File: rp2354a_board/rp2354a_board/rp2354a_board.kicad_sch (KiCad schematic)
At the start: 10 parts, among them J1 USB_B_Micro, U1 RP2350_60QFN, U2 NCP1117-3.3_SOT223

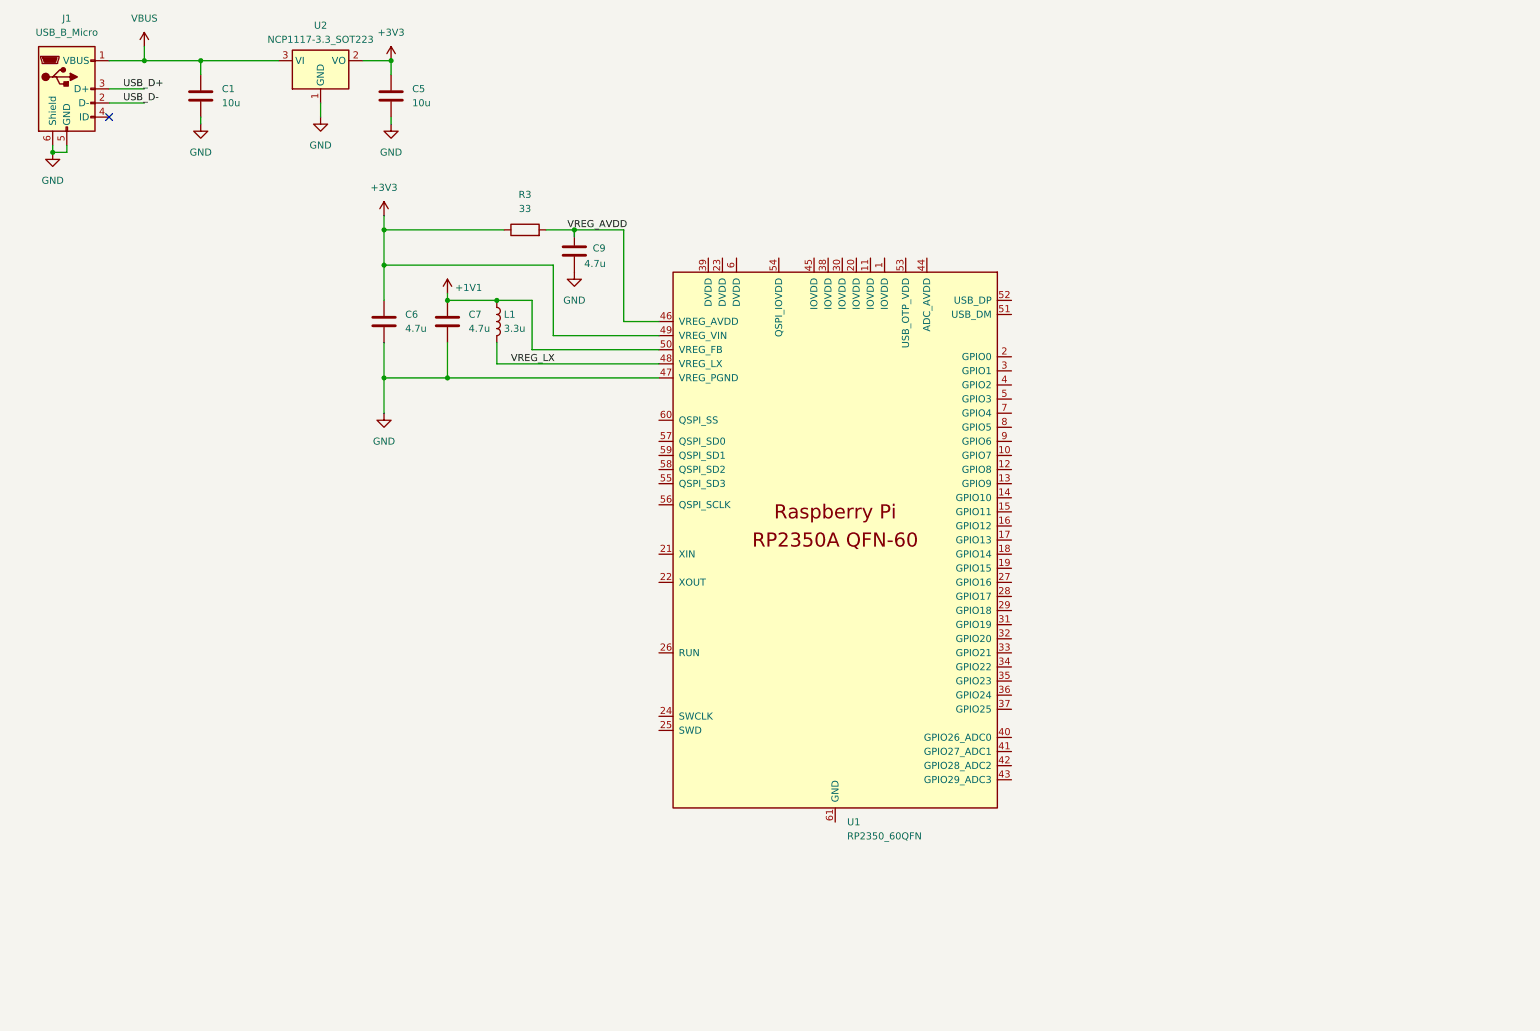
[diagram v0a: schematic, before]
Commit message: Finish schematic for RP235xA board
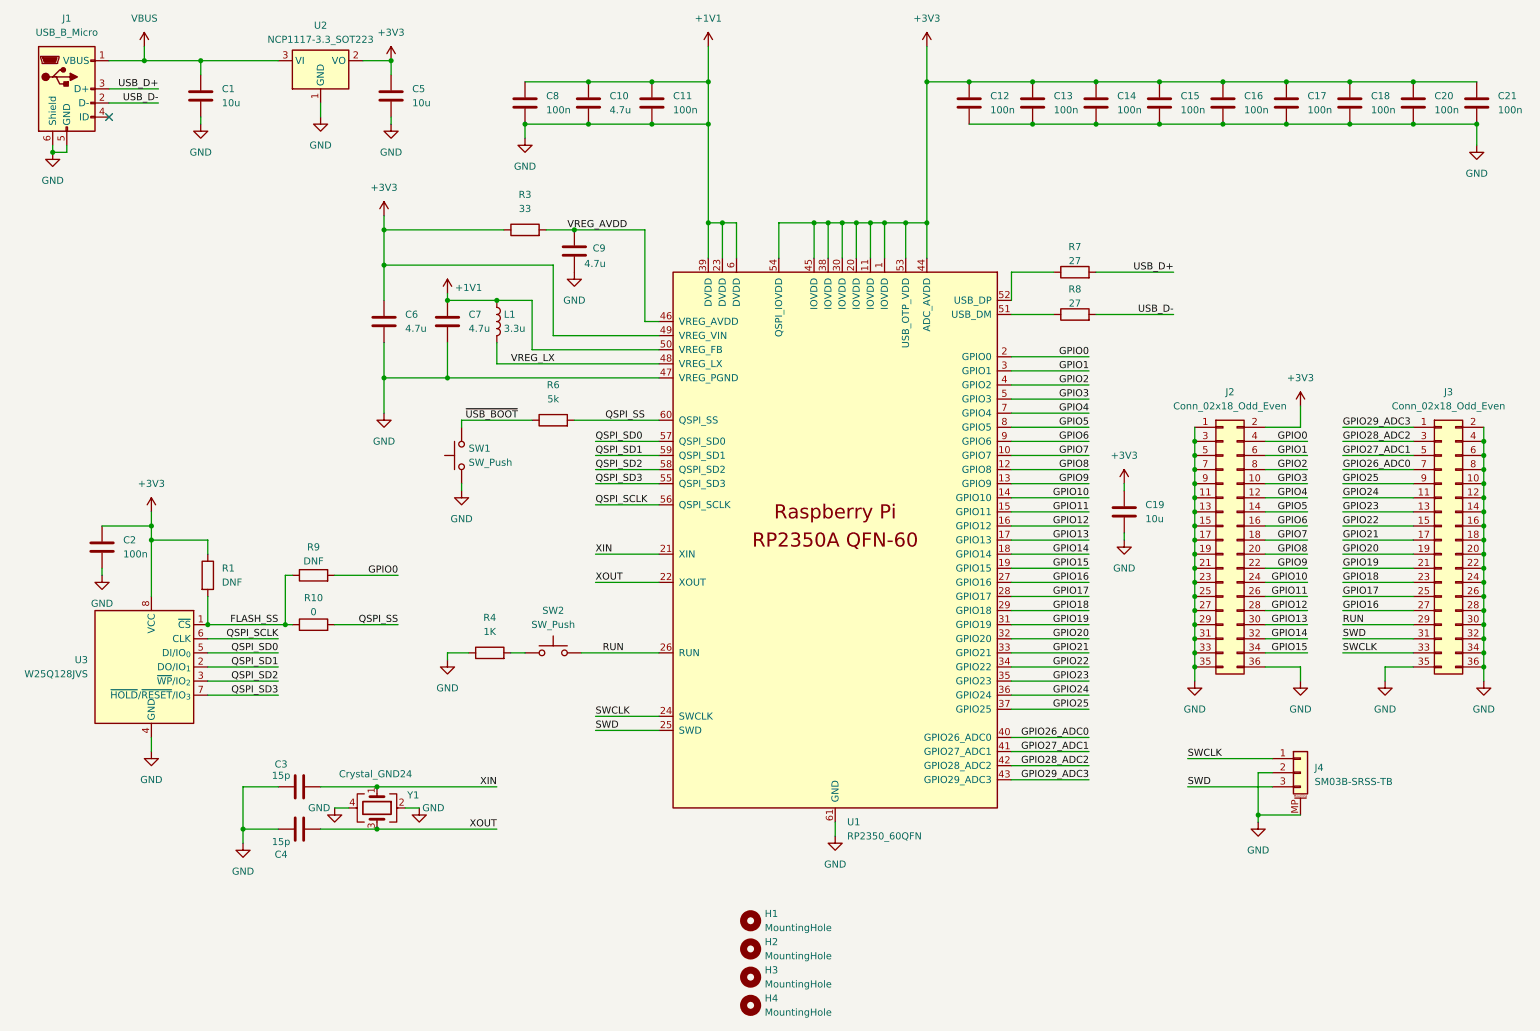
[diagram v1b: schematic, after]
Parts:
- added C10: 4.7u, symbol Device:C
- added C11, C12, C13, C14, C15, C16, C17, C18, C2, C20, C21, C8: 100n, symbol Device:C
- added C19: 10u, symbol Device:C
- added C3, C4: 15p, symbol Device:C
- added H1, H2, H3, H4: MountingHole, MountingHole:MountingHole_2.7mm_M2.5, symbol Mechanical:MountingHole
- added J2, J3: Conn_02x18_Odd_Even, symbol Connector_Generic:Conn_02x18_Odd_Even
- added J4: SM03B-SRSS-TB, Connector_JST:JST_SH_SM03B-SRSS-TB_1x03-1MP_P1.00mm_Horizontal, symbol JST Debug Connector:Conn_01x03_MountingPin
- added R1, R9: DNF, symbol Device:R
- added R10: 0, symbol Device:R
- added R4: 1K, symbol Device:R
- added R6: 5k, symbol Device:R
- added R7, R8: 27, symbol Device:R
- added SW1, SW2: SW_Push, symbol Switch:SW_Push
- added U3: W25Q128JVS, Package_SO:SOIC-8_5.3x5.3mm_P1.27mm, symbol Memory_Flash:W25Q128JVS
- added Y1: Crystal_GND24, symbol Device:Crystal_GND24
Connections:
- net GND is gone; now on net +1V1: C1.2, C5.2, C6.2, C7.2, C9.2, J1.5 (GND), J1.6 (Shield), U1.47 (VREG_PGND), U2.1 (GND)
- net +1V1: now also U1.23 (DVDD), U1.39 (DVDD), U1.6 (DVDD), U1.61 (GND), C10.1, C10.2, C11.1, C11.2, C12.2, C13.2, C14.2, C15.2, C16.2, C17.2, C18.2, C19.2, C2.2, C20.2, C21.2, C3.1, C4.1, C8.1, C8.2, J2.1 (Pin_1), J2.11 (Pin_11), J2.13 (Pin_13), J2.15 (Pin_15), J2.17 (Pin_17), J2.19 (Pin_19), J2.21 (Pin_21), J2.23 (Pin_23), J2.25 (Pin_25), J2.27 (Pin_27), J2.29 (Pin_29), J2.3 (Pin_3), J2.31 (Pin_31), J2.33 (Pin_33), J2.35 (Pin_35), J2.36 (Pin_36), J2.5 (Pin_5), J2.7 (Pin_7), J2.9 (Pin_9), J3.10 (Pin_10), J3.12 (Pin_12), J3.14 (Pin_14), J3.16 (Pin_16), J3.18 (Pin_18), J3.2 (Pin_2), J3.20 (Pin_20), J3.22 (Pin_22), J3.24 (Pin_24), J3.26 (Pin_26), J3.28 (Pin_28), J3.30 (Pin_30), J3.32 (Pin_32), J3.34 (Pin_34), J3.35 (Pin_35), J3.36 (Pin_36), J3.4 (Pin_4), J3.6 (Pin_6), J3.8 (Pin_8), J4.2 (Pin_2), J4.MP (MountPin), R4.1, SW1.1, U3.4 (GND), Y1.2, Y1.4
- net +3V3: now also U1.1 (IOVDD), U1.11 (IOVDD), U1.20 (IOVDD), U1.30 (IOVDD), U1.38 (IOVDD), U1.44 (ADC_AVDD), U1.45 (IOVDD), U1.53 (USB_OTP_VDD), U1.54 (QSPI_IOVDD), C12.1, C13.1, C14.1, C15.1, C16.1, C17.1, C18.1, C19.1, C2.1, C20.1, C21.1, J2.2 (Pin_2), R1.1, U3.8 (VCC)
- net USB_D+: now also R7.2
- net USB_D-: now also R8.2
- net GPIO7: now reaches U1.10 (GPIO7)
- net GPIO7: now also J2.18 (Pin_18)
- net GPIO8: now reaches U1.12 (GPIO8)
- net GPIO8: now also J2.20 (Pin_20)
- net GPIO9: now reaches U1.13 (GPIO9)
- net GPIO9: now also J2.22 (Pin_22)
- net GPIO10: now reaches U1.14 (GPIO10)
- net GPIO10: now also J2.24 (Pin_24)
- net GPIO11: now reaches U1.15 (GPIO11)
- net GPIO11: now also J2.26 (Pin_26)
- net GPIO12: now reaches U1.16 (GPIO12)
- net GPIO12: now also J2.28 (Pin_28)
- net GPIO13: now reaches U1.17 (GPIO13)
- net GPIO13: now also J2.30 (Pin_30)
- net GPIO14: now reaches U1.18 (GPIO14)
- net GPIO14: now also J2.32 (Pin_32)
- net GPIO15: now reaches U1.19 (GPIO15)
- net GPIO15: now also J2.34 (Pin_34)
- net GPIO0: now reaches U1.2 (GPIO0)
- net GPIO0: now also J2.4 (Pin_4), R9.2
- net XIN: now reaches U1.21 (XIN)
- net XIN: now also C3.2, Y1.1
- net XOUT: now reaches U1.22 (XOUT)
- net XOUT: now also C4.2, Y1.3
- net SWCLK: now reaches U1.24 (SWCLK)
- net SWCLK: now also J3.33 (Pin_33), J4.1 (Pin_1)
- net SWD: now reaches U1.25 (SWD)
- net SWD: now also J3.31 (Pin_31), J4.3 (Pin_3)
- net RUN: now reaches U1.26 (RUN)
- net RUN: now also J3.29 (Pin_29), SW2.2
- net GPIO16: now reaches U1.27 (GPIO16)
- net GPIO16: now also J3.27 (Pin_27)
- net GPIO17: now reaches U1.28 (GPIO17)
- net GPIO17: now also J3.25 (Pin_25)
- net GPIO18: now reaches U1.29 (GPIO18)
- net GPIO18: now also J3.23 (Pin_23)
- net GPIO1: now reaches U1.3 (GPIO1)
- net GPIO1: now also J2.6 (Pin_6)
- net GPIO19: now reaches U1.31 (GPIO19)
- net GPIO19: now also J3.21 (Pin_21)
- net GPIO20: now reaches U1.32 (GPIO20)
- net GPIO20: now also J3.19 (Pin_19)
- net GPIO21: now reaches U1.33 (GPIO21)
- net GPIO21: now also J3.17 (Pin_17)
- net GPIO22: now reaches U1.34 (GPIO22)
- net GPIO22: now also J3.15 (Pin_15)
- net GPIO23: now reaches U1.35 (GPIO23)
- net GPIO23: now also J3.13 (Pin_13)
- net GPIO24: now reaches U1.36 (GPIO24)
- net GPIO24: now also J3.11 (Pin_11)
- net GPIO25: now reaches U1.37 (GPIO25)
- net GPIO25: now also J3.9 (Pin_9)
- net GPIO2: now reaches U1.4 (GPIO2)
- net GPIO2: now also J2.8 (Pin_8)
- net GPIO26_ADC0: now reaches U1.40 (GPIO26_ADC0)
- net GPIO26_ADC0: now also J3.7 (Pin_7)
- net GPIO27_ADC1: now reaches U1.41 (GPIO27_ADC1)
- net GPIO27_ADC1: now also J3.5 (Pin_5)
- net GPIO28_ADC2: now reaches U1.42 (GPIO28_ADC2)
- net GPIO28_ADC2: now also J3.3 (Pin_3)
- net GPIO29_ADC3: now reaches U1.43 (GPIO29_ADC3)
- net GPIO29_ADC3: now also J3.1 (Pin_1)
- net GPIO3: now reaches U1.5 (GPIO3)
- net GPIO3: now also J2.10 (Pin_10)
- net at U1.51 (USB_DM): now also R8.1
- net at U1.52 (USB_DP): now also R7.1
- net QSPI_SD3: now reaches U1.55 (QSPI_SD3)
- net QSPI_SD3: now also U3.7 (~{HOLD}/~{RESET}/IO_{3})
- net QSPI_SCLK: now reaches U1.56 (QSPI_SCLK)
- net QSPI_SCLK: now also U3.6 (CLK)
- net QSPI_SD0: now reaches U1.57 (QSPI_SD0)
- net QSPI_SD0: now also U3.5 (DI/IO_{0})
- net QSPI_SD2: now reaches U1.58 (QSPI_SD2)
- net QSPI_SD2: now also U3.3 (~{WP}/IO_{2})
- net QSPI_SD1: now reaches U1.59 (QSPI_SD1)
- net QSPI_SD1: now also U3.2 (DO/IO_{1})
- net QSPI_SS: now reaches U1.60 (QSPI_SS)
- net QSPI_SS: now also R10.2, R6.2
- net GPIO4: now reaches U1.7 (GPIO4)
- net GPIO4: now also J2.12 (Pin_12)
- net GPIO5: now reaches U1.8 (GPIO5)
- net GPIO5: now also J2.14 (Pin_14)
- net GPIO6: now reaches U1.9 (GPIO6)
- net GPIO6: now also J2.16 (Pin_16)
- new net: R4.2, SW2.1
- new net FLASH_SS: R1.2, R10.1, R9.1, U3.1 (~{CS})
- new net ~{USB_BOOT}: R6.1, SW1.2
